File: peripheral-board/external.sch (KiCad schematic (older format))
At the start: 2 parts

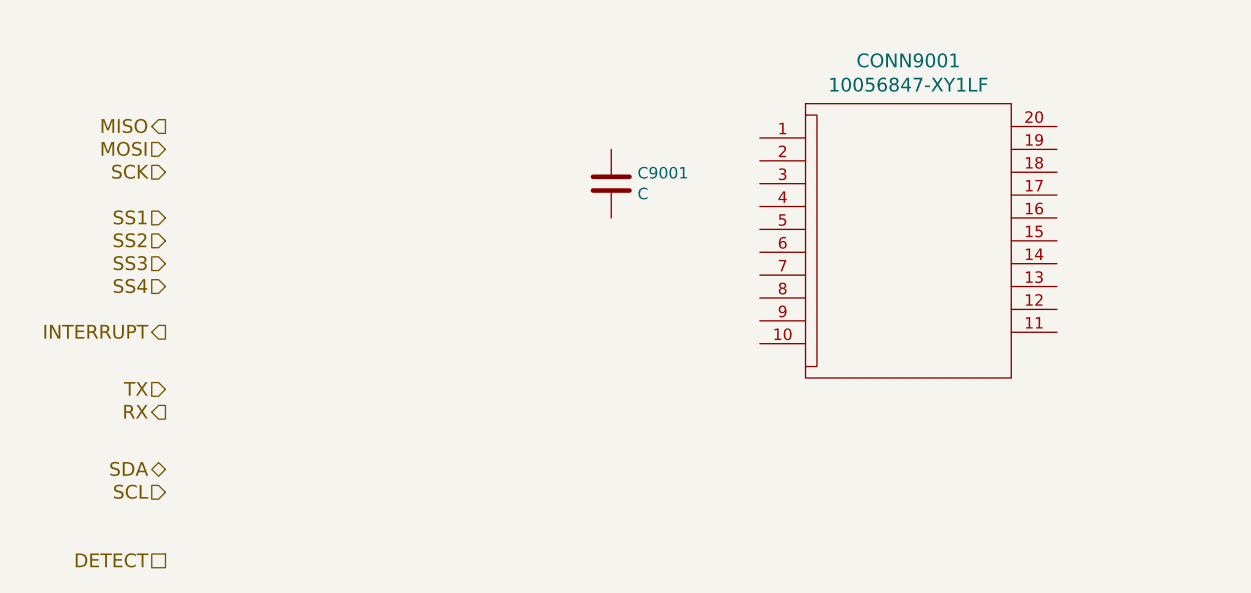
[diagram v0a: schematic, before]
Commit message: power supply component placement
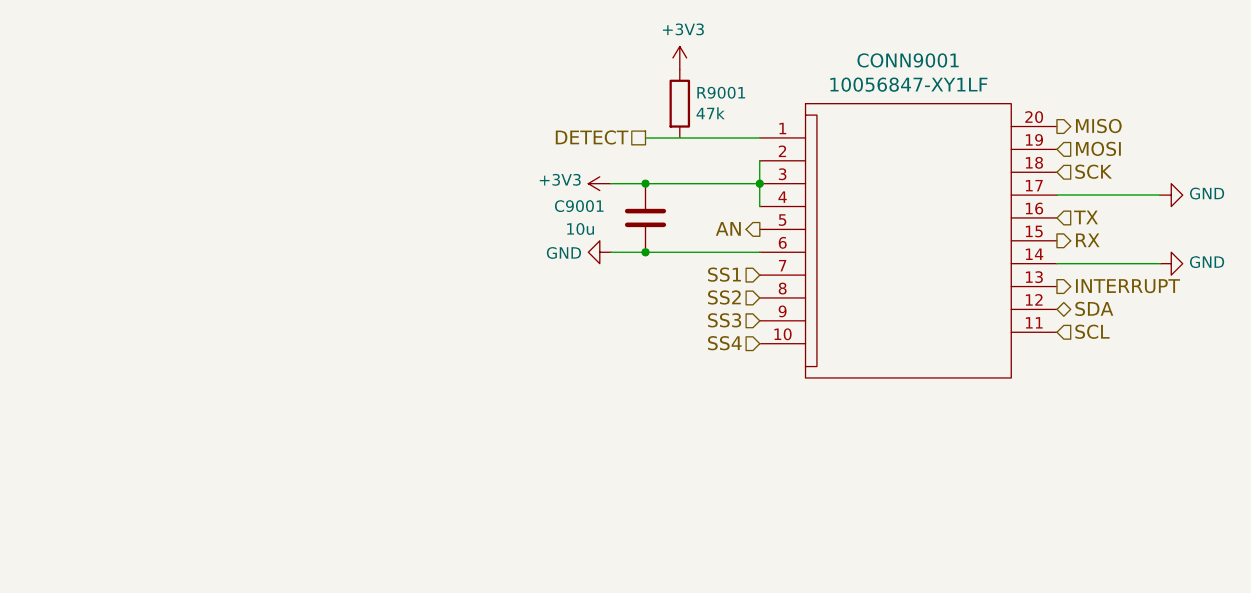
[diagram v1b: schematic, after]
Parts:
- added R9001: 47k, Resistors_SMD:R_0805, symbol R
- C9001: value C -> 10u
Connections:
- net DETECT: now also CONN9001.1
- net INTERRUPT: now also CONN9001.13
- net MISO: now also CONN9001.20
- net MOSI: now also CONN9001.19
- net RX: now also CONN9001.15
- net SCK: now also CONN9001.18
- net SCL: now also CONN9001.11
- net SDA: now also CONN9001.12
- net SS1: now also CONN9001.7
- net SS2: now also CONN9001.8
- net SS3: now also CONN9001.9
- net SS4: now also CONN9001.10
- net TX: now also CONN9001.16
- net GND: now reaches CONN9001.14
- net GND: now also C9001.2, CONN9001.17, CONN9001.6
- net +3V3: now reaches CONN9001.2
- net +3V3: now also C9001.1, CONN9001.3, CONN9001.4, R9001.1
- net AN: now reaches CONN9001.5
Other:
- moved on the sheet: C9001
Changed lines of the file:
@@
 	1    0    0    -1
 $EndComp
-Text HLabel 2300 1650 0    60   Output ~ 0
+Text HLabel 6200 1650 2    60   Output ~ 0
 MISO
-Text HLabel 2300 1750 0    60   Input ~ 0
+Text HLabel 6200 1750 2    60   Input ~ 0
 MOSI
-Text HLabel 2300 1850 0    60   Input ~ 0
+Text HLabel 6200 1850 2    60   Input ~ 0
 SCK
-Text HLabel 2300 2050 0    60   Input ~ 0
+Text HLabel 4900 2300 0    60   Input ~ 0
 SS1
-Text HLabel 2300 2150 0    60   Input ~ 0
+Text HLabel 4900 2400 0    60   Input ~ 0
 SS2
-Text HLabel 2300 2250 0    60   Input ~ 0
+Text HLabel 4900 2500 0    60   Input ~ 0
 SS3
-Text HLabel 2300 2350 0    60   Input ~ 0
+Text HLabel 4900 2600 0    60   Input ~ 0
 SS4
-Text HLabel 2300 2550 0    60   Output ~ 0
+Text HLabel 6200 2350 2    60   Output ~ 0
 INTERRUPT
-Text HLabel 2300 2800 0    60   Input ~ 0
+Text HLabel 6200 2050 2    60   Input ~ 0
 TX
-Text HLabel 2300 2900 0    60   Output ~ 0
+Text HLabel 6200 2150 2    60   Output ~ 0
 RX
-Text HLabel 2300 3150 0    60   BiDi ~ 0
+Text HLabel 6200 2450 2    60   BiDi ~ 0
 SDA
-Text HLabel 2300 3250 0    60   Input ~ 0
+Text HLabel 6200 2550 2    60   Input ~ 0
 SCL
-Text HLabel 2300 3550 0    60   UnSpc ~ 0
+Text HLabel 4400 1700 0    60   UnSpc ~ 0
 DETECT
 $Comp
 L C C9001
 U 1 1 58246CCC
-P 4250 1900
-F 0 "C9001" H 4365 1946 50  0000 L CNN
-F 1 "C" H 4365 1855 50  0000 L CNN
-F 2 "" H 4288 1750 50  0001 C CNN
-F 3 "" H 4250 1900 50  0000 C CNN
-	1    4250 1900
+P 4400 2050
+F 0 "C9001" H 4000 2100 50  0000 L CNN
+F 1 "10u" H 4050 2000 50  0000 L CNN
+F 2 "" H 4438 1900 50  0001 C CNN
+F 3 "" H 4400 2050 50  0000 C CNN
+	1    4400 2050
 	1    0    0    -1
 $EndComp
+$Comp
+L +3V3 #PWR9002
+U 1 1 58A3C2FE
+P 4250 1900
+F 0 "#PWR9002" H -300 800 50  0001 C CNN
+F 1 "+3V3" V 4265 2028 50  0000 L CNN
+F 2 "" H -300 950 50  0001 C CNN
+F 3 "" H -300 950 50  0001 C CNN
+	1    4250 1900
+	0    -1   -1   0
+$EndComp
+$Comp
+L GND #PWR9004
+U 1 1 58A3C347
+P 4250 2200
+F 0 "#PWR9004" H -700 1000 50  0001 C CNN
+F 1 "GND" V 4255 2072 50  0000 R CNN
+F 2 "" H -700 1250 50  0001 C CNN
+F 3 "" H -700 1250 50  0001 C CNN
+	1    4250 2200
+	0    1    1    0
+$EndComp
+$Comp
+L GND #PWR9003
+U 1 1 58A3DB73
+P 6650 1950
+F 0 "#PWR9003" H 1700 750 50  0001 C CNN
+F 1 "GND" V 6655 1822 50  0000 R CNN
+F 2 "" H 1700 1000 50  0001 C CNN
+F 3 "" H 1700 1000 50  0001 C CNN
+	1    6650 1950
+	0    -1   -1   0
+$EndComp
+$Comp
+L GND #PWR9005
+U 1 1 58A3DB88
+P 6650 2250
+F 0 "#PWR9005" H 1700 1050 50  0001 C CNN
+F 1 "GND" V 6655 2122 50  0000 R CNN
+F 2 "" H 1700 1300 50  0001 C CNN
+F 3 "" H 1700 1300 50  0001 C CNN
+	1    6650 2250
+	0    -1   -1   0
+$EndComp
+Wire Wire Line
+	6650 1950 6200 1950
+Wire Wire Line
+	6650 2250 6200 2250
+Text HLabel 4900 2100 0    60   Output ~ 0
+AN
+Wire Wire Line
+	4900 1800 4900 2000
+Connection ~ 4900 1900
+Wire Wire Line
+	4250 1900 4900 1900
+Connection ~ 4400 1900
+Wire Wire Line
+	4250 2200 4900 2200
+Connection ~ 4400 2200
+Wire Wire Line
+	4900 1700 4400 1700
+$Comp
+L R R9001
+U 1 1 58A5EC2B
+P 4550 1550
+F 0 "R9001" H 4620 1596 50  0000 L CNN
+F 1 "47k" H 4620 1505 50  0000 L CNN
+F 2 "Resistors_SMD:R_0805" V -370 200 50  0001 C CNN
+F 3 "" H -300 200 50  0001 C CNN
+	1    4550 1550
+	1    0    0    -1
+$EndComp
+$Comp
+L +3V3 #PWR9001
+U 1 1 58A5EC6F
+P 4550 1400
+F 0 "#PWR9001" H -400 -200 50  0001 C CNN
+F 1 "+3V3" H 4565 1573 50  0000 C CNN
+F 2 "" H -400 -50 50  0001 C CNN
+F 3 "" H -400 -50 50  0001 C CNN
+	1    4550 1400
+	1    0    0    -1
+$EndComp

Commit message: routed spi
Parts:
- C9001: footprint (none) -> Capacitors_SMD:C_1206
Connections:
- net MOSI: now also CONN9001.18; no longer CONN9001.19
- net SCK: now also CONN9001.19; no longer CONN9001.18
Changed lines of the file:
@@
 Text HLabel 6200 1650 2    60   Output ~ 0
 MISO
+Text HLabel 6200 1850 2    60   Input ~ 0
+MOSI
 Text HLabel 6200 1750 2    60   Input ~ 0
-MOSI
-Text HLabel 6200 1850 2    60   Input ~ 0
 SCK
 Text HLabel 4900 2300 0    60   Input ~ 0
@@
 F 0 "C9001" H 4000 2100 50  0000 L CNN
 F 1 "10u" H 4050 2000 50  0000 L CNN
-F 2 "" H 4438 1900 50  0001 C CNN
+F 2 "Capacitors_SMD:C_1206" H 4438 1900 50  0001 C CNN
 F 3 "" H 4400 2050 50  0000 C CNN
 	1    4400 2050
@@
 $EndComp
 $Comp
-L +3V3 #PWR082
+L +3V3 #PWR086
 U 1 1 58A3C2FE
 P 4250 1900
-F 0 "#PWR082" H -300 800 50  0001 C CNN
+F 0 "#PWR086" H -300 800 50  0001 C CNN
 F 1 "+3V3" V 4265 2028 50  0000 L CNN
 F 2 "" H -300 950 50  0001 C CNN
@@
 $EndComp
 $Comp
-L GND #PWR083
+L GND #PWR087
 U 1 1 58A3C347
 P 4250 2200
-F 0 "#PWR083" H -700 1000 50  0001 C CNN
+F 0 "#PWR087" H -700 1000 50  0001 C CNN
 F 1 "GND" V 4255 2072 50  0000 R CNN
 F 2 "" H -700 1250 50  0001 C CNN
@@
 $EndComp
 $Comp
-L GND #PWR084
+L GND #PWR088
 U 1 1 58A3DB73
 P 6650 1950
-F 0 "#PWR084" H 1700 750 50  0001 C CNN
+F 0 "#PWR088" H 1700 750 50  0001 C CNN
 F 1 "GND" V 6655 1822 50  0000 R CNN
 F 2 "" H 1700 1000 50  0001 C CNN
@@
 $EndComp
 $Comp
-L GND #PWR085
+L GND #PWR089
 U 1 1 58A3DB88
 P 6650 2250
-F 0 "#PWR085" H 1700 1050 50  0001 C CNN
+F 0 "#PWR089" H 1700 1050 50  0001 C CNN
 F 1 "GND" V 6655 2122 50  0000 R CNN
 F 2 "" H 1700 1300 50  0001 C CNN
@@
 $EndComp
 $Comp
-L +3V3 #PWR086
+L +3V3 #PWR090
 U 1 1 58A5EC6F
 P 4550 1400
-F 0 "#PWR086" H -400 -200 50  0001 C CNN
+F 0 "#PWR090" H -400 -200 50  0001 C CNN
 F 1 "+3V3" H 4565 1573 50  0000 C CNN
 F 2 "" H -400 -50 50  0001 C CNN

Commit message: routed misc signals to micro
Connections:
- net DETECT: now also R9001.2
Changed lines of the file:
@@
 $EndComp
 $Comp
-L +3V3 #PWR094
+L +3V3 #PWR9002
 U 1 1 58A3C2FE
 P 4250 1900
-F 0 "#PWR094" H -300 800 50  0001 C CNN
+F 0 "#PWR9002" H -300 800 50  0001 C CNN
 F 1 "+3V3" V 4265 2028 50  0000 L CNN
 F 2 "" H -300 950 50  0001 C CNN
@@
 $EndComp
 $Comp
-L GND #PWR095
+L GND #PWR9004
 U 1 1 58A3C347
 P 4250 2200
-F 0 "#PWR095" H -700 1000 50  0001 C CNN
+F 0 "#PWR9004" H -700 1000 50  0001 C CNN
 F 1 "GND" V 4255 2072 50  0000 R CNN
 F 2 "" H -700 1250 50  0001 C CNN
@@
 $EndComp
 $Comp
-L GND #PWR096
+L GND #PWR9003
 U 1 1 58A3DB73
 P 6650 1950
-F 0 "#PWR096" H 1700 750 50  0001 C CNN
+F 0 "#PWR9003" H 1700 750 50  0001 C CNN
 F 1 "GND" V 6655 1822 50  0000 R CNN
 F 2 "" H 1700 1000 50  0001 C CNN
@@
 $EndComp
 $Comp
-L GND #PWR097
+L GND #PWR9005
 U 1 1 58A3DB88
 P 6650 2250
-F 0 "#PWR097" H 1700 1050 50  0001 C CNN
+F 0 "#PWR9005" H 1700 1050 50  0001 C CNN
 F 1 "GND" V 6655 2122 50  0000 R CNN
 F 2 "" H 1700 1300 50  0001 C CNN
@@
 	4250 2200 4900 2200
 Connection ~ 4400 2200
-Wire Wire Line
-	4900 1700 4400 1700
 $Comp
 L R R9001
@@
 $EndComp
 $Comp
-L +3V3 #PWR098
+L +3V3 #PWR9001
 U 1 1 58A5EC6F
 P 4550 1400
-F 0 "#PWR098" H -400 -200 50  0001 C CNN
+F 0 "#PWR9001" H -400 -200 50  0001 C CNN
 F 1 "+3V3" H 4565 1573 50  0000 C CNN
 F 2 "" H -400 -50 50  0001 C CNN
@@
 	1    0    0    -1
 $EndComp
+Wire Wire Line
+	4400 1700 4900 1700
+Connection ~ 4550 1700
 $EndSCHEMATC
